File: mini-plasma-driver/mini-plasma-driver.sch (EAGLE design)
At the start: 83 parts, among them IC1 IR21844D, IC2 74LS19N, IC3 NE555N, IC4 NCP781IC, IC5 IR21844D, Q1 IRF640, Q2 IRF640, Q3 2N2369, Q4 2N2369, Q5 IRF640, Q6 IRF640

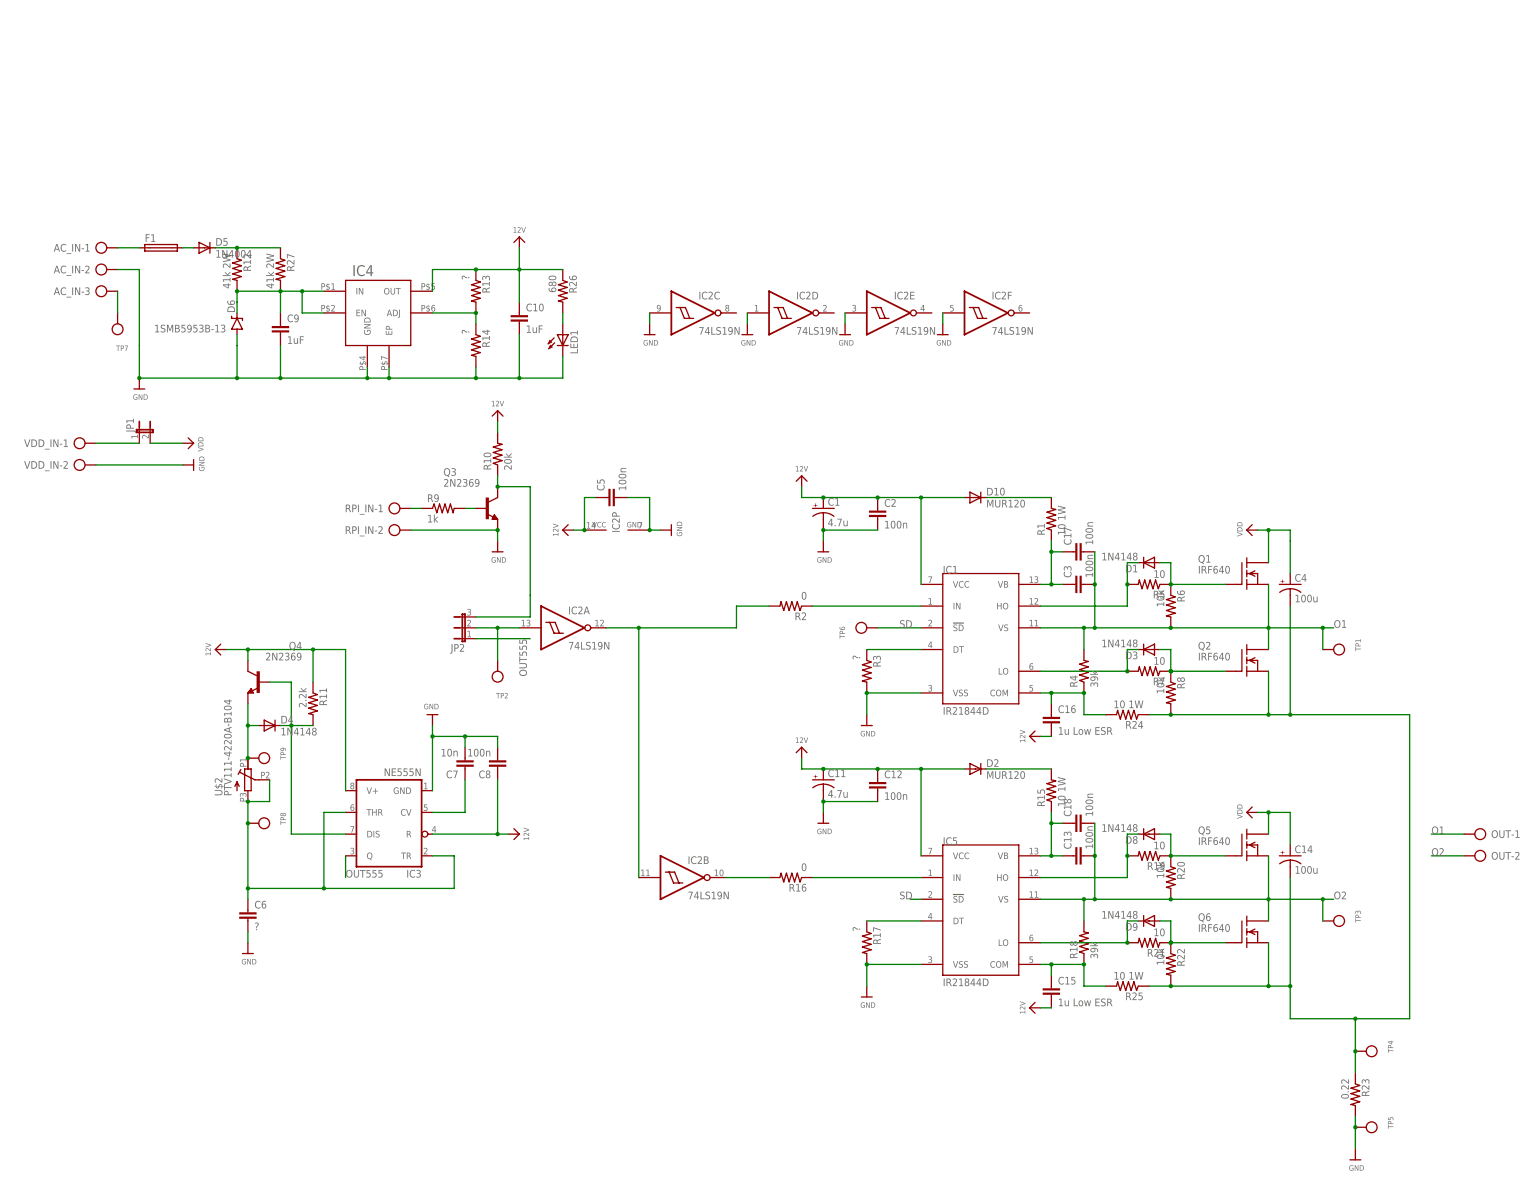
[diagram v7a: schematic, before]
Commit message: removed 12v PS, added TO-247 footprints, checked all packages
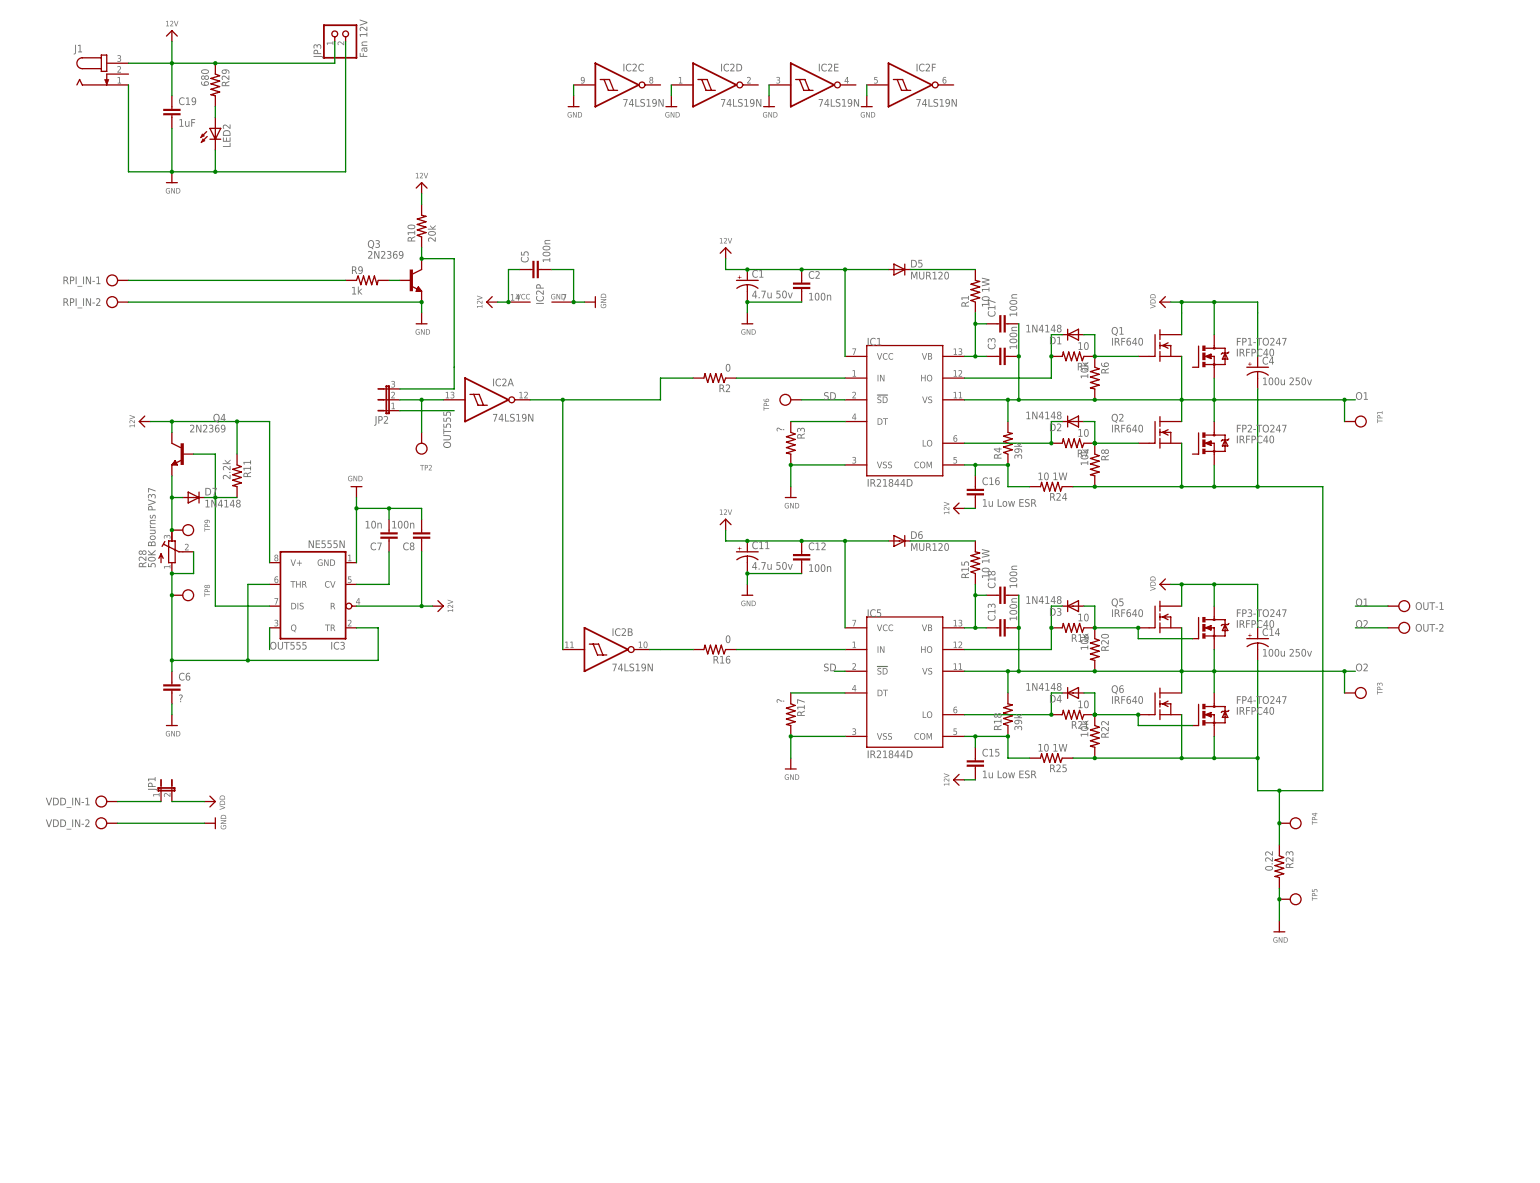
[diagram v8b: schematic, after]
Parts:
- removed AC_IN: (no value), con-ptr500:AK500/3
- removed C10, C9: 1uF, rcl:C-EU025-025X050
- removed D10: MUR120, diode:MUR150RL
- removed D8, D9: 1N4148, diode:1N4148DO35-10
- removed F1: (no value), fuse:SH22,5A
- removed IC4: NCP781IC, keves-ng:NCP781IC
- removed LED1: (no value), led:LED5MM
- removed R12, R27: 41k 2W, rcl:R-US_0207/10
- removed R13, R14: ?, rcl:R-US_0207/10
- removed R26: 680, rcl:R-US_0207/10
- removed TP7: (no value), microbuilder:TESTPOINT0.1"
- removed U$2: PTV111-4220A-B104, keves:PTV111-4220A-B104
- added C19: 1uF, rcl:C-EU025-025X050
- added D7: 1N4148, diode:1N4148DO35-10
- added FP1-TO247, FP2-TO247, FP3-TO247, FP4-TO247: IRFPC40, transistor-power:IRFPC40
- added J1: (no value), con-jack:JACK-PLUG0
- added JP3: Fan 12V, pinhead:PINHD-1X2
- added LED2: (no value), led:LED5MM
- added R28: 50K Bourns PV37, rcl:R-TRIMM3296Y
- added R29: 680, rcl:R-US_0207/10
- C1, C11: value 4.7u -> 4.7u 50v; device rcl:CPOL-USE2.5-5 -> rcl:CPOL-USE2-5
- C13, C17, C18, C2, C3, C5, C7, C8: device rcl:C-EU025-025X050 -> rcl:C-EU025-030X050
- C14, C4: value 100u -> 100u 250v; device rcl:CPOL-USE3.5-10 -> rcl:CPOL-USE7.5-18
- C15, C16: device rcl:C-EU025-025X050 -> rcl:C-EU050-035X075
- D2: value MUR120 -> 1N4148; device diode:MUR150RL -> diode:1N4148DO35-10
- D5: value 1N4004 -> MUR120; device adafruit:1N4004 -> diode:MUR150RL
- D6: value 1SMB5953B-13 -> MUR120; device SparkFun-DiscreteSemi:DIODE-ZENERSMB -> diode:MUR150RL
- R1, R15: device rcl:R-US_0207/10 -> rcl:R-US_0309/V
- R23: device rcl:R-US_0207/10 -> rcl:R-US_0617/17
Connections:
- removed net N$18: D5.A, F1.2
- removed net N$19: D5.C, R12.1, R27.1
- removed net N$20: C9.1, D6.C, IC4.EN, IC4.IN, R12.2, R27.2
- removed net N$22: IC4.ADJ, R13.2, R14.1
- removed net N$25: AC_IN-3.KL, TP7.P$1
- removed net N$31: AC_IN-1.KL, F1.1
- removed net N$32: LED1.A, R26.2
- new net N$34: LED2.A, R29.2
- net 12V: now also C19.1, D5.A, D6.A, J1.3, JP3.1, R29.1; no longer C10.1, D10.A, D2.A, IC4.OUT, R13.1, R26.1
- net GND: now also C19.2, J1.1, JP3.2, LED2.C; no longer AC_IN-2.KL, C10.2, C9.2, D6.A, IC4.EP, IC4.GND, LED1.C, R14.2
- net N$1: now also D5.C; no longer D10.C
- net N$14: now also D7.C; no longer D4.C
- net N$15: now also R28.A, R28.S; no longer U$2.E, U$2.S
- net N$16: now also D7.A, R28.E; no longer D4.A, U$2.A
- net N$2: now also FP2-TO247.S, FP4-TO247.S
- net N$21: now also D6.C; no longer D2.C
- net N$27: now also D3.C; no longer D8.C
- net N$28: now also D3.A, FP3-TO247.G; no longer D8.A
- net N$29: now also D4.C; no longer D9.C
- net N$30: now also D4.A, FP4-TO247.G; no longer D9.A
- net N$8: now also D2.C; no longer D3.C
- net N$9: now also D2.A; no longer D3.A
- net O1: now also FP1-TO247.S, FP2-TO247.D
- net O2: now also FP3-TO247.S, FP4-TO247.D
- net VDD: now also FP1-TO247.D, FP3-TO247.D
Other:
- moved on the sheet: C1, C11, C12, C13, C14, C15, C16, C17, C18, C2, C3, C4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
